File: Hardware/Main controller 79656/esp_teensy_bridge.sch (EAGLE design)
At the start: 101 parts, among them IC2 PBQ79656PAPTQ1, Q5 VISHAY_SIS862DN-T1-GE3VISHAY_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, Q6 VISHAY_SIS862DN-T1-GE3VISHAY_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, Q7 VISHAY_SIS862DN-T1-GE3VISHAY_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, Q8 VISHAY_SIS862DN-T1-GE3VISHAY_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, T2 PBHV8115X, 115, U1 MCP2562-E/SN, U2 ESP32-DEVKITC-32D, X1 5566-12

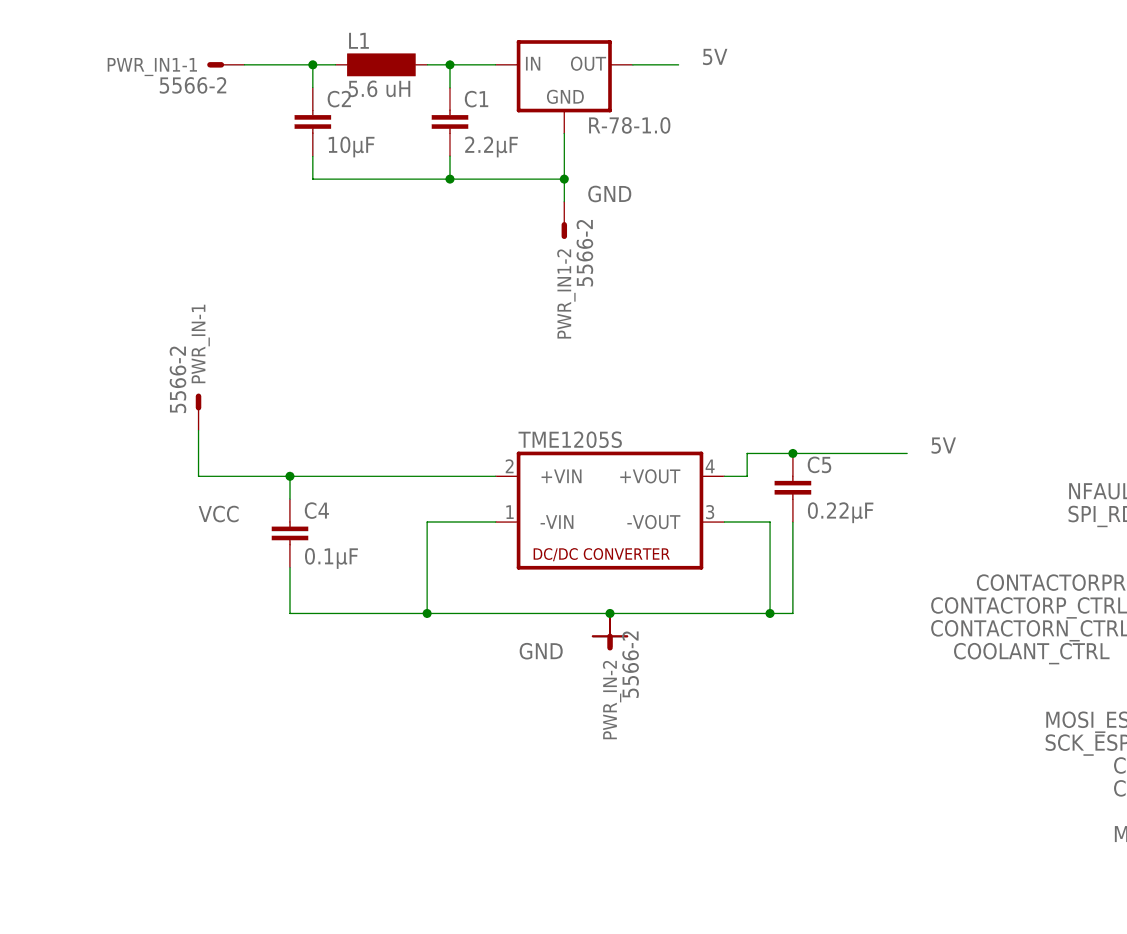
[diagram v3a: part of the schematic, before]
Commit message: buck converter layout
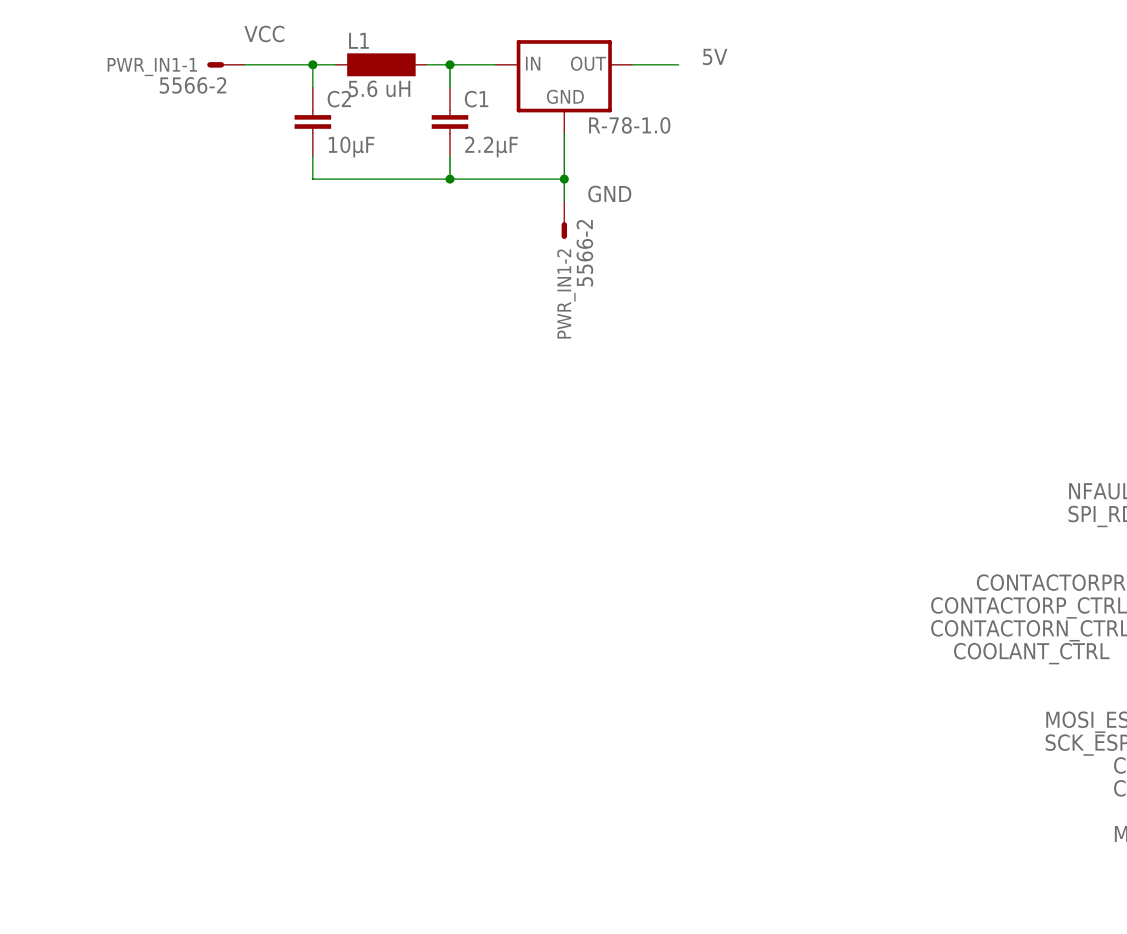
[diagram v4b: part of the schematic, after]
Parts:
- removed C4: 0.1μF, rcl:C-EUC0603
- removed C5: 0.22μF, rcl:C-EUC0603
- removed PWR_IN: 5566-2, con-molex:5566-2
- removed TME1205S: (no value), dc-dc-converter:NME
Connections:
- removed net N$36: C2.1, L1.1, PWR_IN1-1.S
- net 5V: no longer C5.1, TME1205S.+VOUT
- net GND: no longer C4.2, C5.2, PWR_IN-2.S, TME1205S.-VIN, TME1205S.-VOUT
- net VCC: now also C2.1, L1.1, PWR_IN1-1.S; no longer C4.1, PWR_IN-1.S, TME1205S.+VIN
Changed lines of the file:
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@@
 </classes>
 <parts>
-<part name="TME1205S" library="dc-dc-converter" library_urn="urn:adsk.eagle:library:208" deviceset="NME" device="" package3d_urn="urn:adsk.eagle:package:12313/1"/>
-<part name="GND1" library="supply1" library_urn="urn:adsk.eagle:library:371" deviceset="GND" device=""/>
-<part name="C5" library="rcl" library_urn="urn:adsk.eagle:library:334" deviceset="C-EU" device="C0603" package3d_urn="urn:adsk.eagle:package:23616/2" value="0.22μF"/>
-<part name="C4" library="rcl" library_urn="urn:adsk.eagle:library:334" deviceset="C-EU" device="C0603" package3d_urn="urn:adsk.eagle:package:23616/2" value="0.1μF"/>
-<part name="PWR_IN" library="con-molex" library_urn="urn:adsk.eagle:library:165" deviceset="5566-2" device="" package3d_urn="urn:adsk.eagle:package:8078583/1"/>
 <part name="COOLANT" library="con-molex" library_urn="urn:adsk.eagle:library:165" deviceset="5566-2" device="" package3d_urn="urn:adsk.eagle:package:8078583/1"/>
 <part name="CONTACTOR_N" library="con-molex" library_urn="urn:adsk.eagle:library:165" deviceset="5566-2" device="" package3d_urn="urn:adsk.eagle:package:8078583/1"/>
@@
 </plain>
 <instances>
-<instance part="TME1205S" gate="G$1" x="-30.48" y="111.76" smashed="yes">
-<attribute name="NAME" x="-40.64" y="117.475" size="1.778" layer="95"/>
-<attribute name="VALUE" x="-40.64" y="101.6" size="1.778" layer="96"/>
-</instance>
-<instance part="GND1" gate="1" x="-30.48" y="96.52" smashed="yes">
-<attribute name="VALUE" x="-40.64" y="93.98" size="1.778" layer="96"/>
-</instance>
-<instance part="C5" gate="G$1" x="-10.16" y="114.3" smashed="yes">
-<attribute name="NAME" x="-8.636" y="114.681" size="1.778" layer="95"/>
-<attribute name="VALUE" x="-8.636" y="109.601" size="1.778" layer="96"/>
-</instance>
-<instance part="C4" gate="G$1" x="-66.04" y="109.22" smashed="yes">
-<attribute name="NAME" x="-64.516" y="109.601" size="1.778" layer="95"/>
-<attribute name="VALUE" x="-64.516" y="104.521" size="1.778" layer="96"/>
-</instance>
-<instance part="PWR_IN" gate="-1" x="-76.2" y="121.92" smashed="yes" rot="R90">
-<attribute name="NAME" x="-75.438" y="124.46" size="1.524" layer="95" rot="R90"/>
-<attribute name="VALUE" x="-77.597" y="121.158" size="1.778" layer="96" rot="R90"/>
-</instance>
-<instance part="PWR_IN" gate="-2" x="-30.48" y="96.52" smashed="yes" rot="R270">
-<attribute name="NAME" x="-31.242" y="93.98" size="1.524" layer="95" rot="R270"/>
-<attribute name="VALUE" x="-29.083" y="97.282" size="1.778" layer="96" rot="R270"/>
-</instance>
 <instance part="COOLANT" gate="-1" x="-119.38" y="71.12" smashed="yes">
 <attribute name="NAME" x="-116.84" y="70.358" size="1.524" layer="95"/>
@@
 <nets>
 <net name="GND" class="0">
-<segment>
-<pinref part="TME1205S" gate="G$1" pin="-VIN"/>
-<wire x1="-50.8" y1="109.22" x2="-43.18" y2="109.22" width="0.1524" layer="91"/>
-<wire x1="-50.8" y1="109.22" x2="-50.8" y2="99.06" width="0.1524" layer="91"/>
-<wire x1="-50.8" y1="99.06" x2="-30.48" y2="99.06" width="0.1524" layer="91"/>
-<wire x1="-30.48" y1="99.06" x2="-12.7" y2="99.06" width="0.1524" layer="91"/>
-<pinref part="GND1" gate="1" pin="GND"/>
-<junction x="-30.48" y="99.06"/>
-<pinref part="C4" gate="G$1" pin="2"/>
-<wire x1="-66.04" y1="104.14" x2="-66.04" y2="99.06" width="0.1524" layer="91"/>
-<wire x1="-66.04" y1="99.06" x2="-50.8" y2="99.06" width="0.1524" layer="91"/>
-<junction x="-50.8" y="99.06"/>
-<pinref part="TME1205S" gate="G$1" pin="-VOUT"/>
-<wire x1="-17.78" y1="109.22" x2="-12.7" y2="109.22" width="0.1524" layer="91"/>
-<wire x1="-12.7" y1="109.22" x2="-12.7" y2="99.06" width="0.1524" layer="91"/>
-<wire x1="-12.7" y1="99.06" x2="-10.16" y2="99.06" width="0.1524" layer="91"/>
-<junction x="-12.7" y="99.06"/>
-<pinref part="C5" gate="G$1" pin="2"/>
-<wire x1="-10.16" y1="99.06" x2="-10.16" y2="109.22" width="0.1524" layer="91"/>
-<pinref part="PWR_IN" gate="-2" pin="S"/>
-</segment>
 <segment>
 <wire x1="-129.54" y1="63.5" x2="-129.54" y2="60.96" width="0.1524" layer="91"/>
@@
 <net name="5V" class="0">
 <segment>
-<pinref part="TME1205S" gate="G$1" pin="+VOUT"/>
-<wire x1="-17.78" y1="114.3" x2="-15.24" y2="114.3" width="0.1524" layer="91"/>
-<wire x1="-15.24" y1="114.3" x2="-15.24" y2="116.84" width="0.1524" layer="91"/>
-<pinref part="C5" gate="G$1" pin="1"/>
-<wire x1="-15.24" y1="116.84" x2="-10.16" y2="116.84" width="0.1524" layer="91"/>
-<wire x1="-10.16" y1="116.84" x2="2.54" y2="116.84" width="0.1524" layer="91"/>
-<junction x="-10.16" y="116.84"/>
-<label x="5.08" y="116.84" size="1.778" layer="95"/>
-</segment>
-<segment>
 <pinref part="U$3" gate="G$1" pin="VIN"/>
 <wire x1="71.12" y1="127" x2="71.12" y2="132.08" width="0.1524" layer="91"/>
@@
 <wire x1="-121.92" y1="-10.16" x2="-124.46" y2="-10.16" width="0.1524" layer="91"/>
 <label x="-124.46" y="-10.16" size="1.778" layer="95"/>
-</segment>
-<segment>
-<wire x1="-76.2" y1="119.38" x2="-76.2" y2="114.3" width="0.1524" layer="91"/>
-<pinref part="TME1205S" gate="G$1" pin="+VIN"/>
-<wire x1="-76.2" y1="114.3" x2="-66.04" y2="114.3" width="0.1524" layer="91"/>
-<pinref part="C4" gate="G$1" pin="1"/>
-<wire x1="-66.04" y1="114.3" x2="-43.18" y2="114.3" width="0.1524" layer="91"/>
-<wire x1="-66.04" y1="111.76" x2="-66.04" y2="114.3" width="0.1524" layer="91"/>
-<junction x="-66.04" y="114.3"/>
-<label x="-76.2" y="109.22" size="1.778" layer="95"/>
-<pinref part="PWR_IN" gate="-1" pin="S"/>
 </segment>
 <segment>
@@
 <wire x1="-60.96" y1="-218.44" x2="-71.12" y2="-218.44" width="0.1524" layer="91"/>
 <label x="-71.12" y="-218.44" size="1.778" layer="95"/>
+</segment>
+<segment>
+<pinref part="C2" gate="G$1" pin="1"/>
+<wire x1="-63.5" y1="157.48" x2="-63.5" y2="160.02" width="0.1524" layer="91"/>
+<pinref part="L1" gate="G$1" pin="1"/>
+<wire x1="-63.5" y1="160.02" x2="-60.96" y2="160.02" width="0.1524" layer="91"/>
+<pinref part="PWR_IN1" gate="-1" pin="S"/>
+<wire x1="-63.5" y1="160.02" x2="-71.12" y2="160.02" width="0.1524" layer="91"/>
+<junction x="-63.5" y="160.02"/>
+<label x="-71.12" y="162.56" size="1.778" layer="95"/>
 </segment>
 </net>
@@
 </segment>
 </net>
-<net name="N$36" class="0">
-<segment>
-<pinref part="C2" gate="G$1" pin="1"/>
-<wire x1="-63.5" y1="157.48" x2="-63.5" y2="160.02" width="0.1524" layer="91"/>
-<pinref part="L1" gate="G$1" pin="1"/>
-<wire x1="-63.5" y1="160.02" x2="-60.96" y2="160.02" width="0.1524" layer="91"/>
-<pinref part="PWR_IN1" gate="-1" pin="S"/>
-<wire x1="-63.5" y1="160.02" x2="-71.12" y2="160.02" width="0.1524" layer="91"/>
-<junction x="-63.5" y="160.02"/>
-</segment>
-</net>

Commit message: Mainboard fixes
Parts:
- removed R-78-1.0: (no value), v-reg:78XXS
- added PS1: R-785.0-1.0, R-785.0-1.0:R-785.0-1.0
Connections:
- net 5V: now also PS1.+VOUT; no longer R-78-1.0.OUT
- net GND: now also PS1.GND, U2.GND2, U2.GND3; no longer R-78-1.0.GND
- net N$16: now also PS1.+VIN; no longer R-78-1.0.IN
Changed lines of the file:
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@@
 <part name="R9" library="rcl" library_urn="urn:adsk.eagle:library:334" deviceset="R-US_" device="R0805" package3d_urn="urn:adsk.eagle:package:23553/2"/>
 <part name="U$1" library="TB0108" deviceset="TXB0108PW" device="SMD"/>
-<part name="R-78-1.0" library="v-reg" library_urn="urn:adsk.eagle:library:409" deviceset="78XXS" device="" package3d_urn="urn:adsk.eagle:package:30342/1"/>
 <part name="C1" library="rcl" library_urn="urn:adsk.eagle:library:334" deviceset="C-EU" device="C0603" package3d_urn="urn:adsk.eagle:package:23616/2" value="2.2μF"/>
 <part name="C2" library="rcl" library_urn="urn:adsk.eagle:library:334" deviceset="C-EU" device="C0603" package3d_urn="urn:adsk.eagle:package:23616/2" value="10μF"/>
 <part name="L1" library="inductor-neosid" library_urn="urn:adsk.eagle:library:241" deviceset="SD8" device="" package3d_urn="urn:adsk.eagle:package:14649/1" value="5.6 uH"/>
 <part name="PWR_IN1" library="con-molex" library_urn="urn:adsk.eagle:library:165" deviceset="5566-2" device="" package3d_urn="urn:adsk.eagle:package:8078583/1"/>
+<part name="PS1" library="R-785.0-1.0" deviceset="R-785.0-1.0" device=""/>
 </parts>
 <sheets>
@@
 <attribute name="VALUE" x="88.9" y="-121.92" size="1.27" layer="96" rot="R180"/>
 </instance>
-<instance part="R-78-1.0" gate="1" x="-35.56" y="160.02" smashed="yes">
-<attribute name="NAME" x="-33.02" y="152.4" size="1.778" layer="95"/>
-<attribute name="VALUE" x="-33.02" y="149.86" size="1.778" layer="96"/>
-</instance>
 <instance part="C1" gate="G$1" x="-48.26" y="154.94" smashed="yes">
 <attribute name="NAME" x="-46.736" y="155.321" size="1.778" layer="95"/>
@@
 <attribute name="NAME" x="-36.322" y="139.7" size="1.524" layer="95" rot="R270"/>
 <attribute name="VALUE" x="-34.163" y="143.002" size="1.778" layer="96" rot="R270"/>
+</instance>
+<instance part="PS1" gate="G$1" x="-33.02" y="170.18" smashed="yes">
+<attribute name="NAME" x="-43.1839" y="176.5379" size="1.77938125" layer="95"/>
+<attribute name="VALUE" x="-43.1814" y="162.5573" size="1.77848125" layer="96"/>
 </instance>
 </instances>
@@
 </segment>
 <segment>
-<pinref part="R-78-1.0" gate="1" pin="GND"/>
-<wire x1="-35.56" y1="152.4" x2="-35.56" y2="147.32" width="0.1524" layer="91"/>
 <wire x1="-35.56" y1="147.32" x2="-48.26" y2="147.32" width="0.1524" layer="91"/>
 <pinref part="C1" gate="G$1" pin="2"/>
@@
 <junction x="-35.56" y="147.32"/>
 <label x="-33.02" y="144.78" size="1.778" layer="95"/>
+<pinref part="PS1" gate="G$1" pin="GND"/>
+<wire x1="-35.56" y1="147.32" x2="-17.78" y2="147.32" width="0.1524" layer="91"/>
+<wire x1="-17.78" y1="147.32" x2="-17.78" y2="167.64" width="0.1524" layer="91"/>
+</segment>
+<segment>
+<pinref part="U2" gate="G$1" pin="GND3"/>
+<wire x1="73.66" y1="7.62" x2="78.74" y2="7.62" width="0.1524" layer="91"/>
+<label x="73.66" y="7.62" size="1.778" layer="95"/>
+</segment>
+<segment>
+<pinref part="U2" gate="G$1" pin="GND2"/>
+<wire x1="73.66" y1="-7.62" x2="78.74" y2="-7.62" width="0.1524" layer="91"/>
+<label x="73.66" y="-7.62" size="1.778" layer="95"/>
 </segment>
 </net>
@@
 </segment>
 <segment>
-<pinref part="R-78-1.0" gate="1" pin="OUT"/>
 <wire x1="-27.94" y1="160.02" x2="-22.86" y2="160.02" width="0.1524" layer="91"/>
 <label x="-20.32" y="160.02" size="1.778" layer="95"/>
+<pinref part="PS1" gate="G$1" pin="+VOUT"/>
+<wire x1="-27.94" y1="160.02" x2="-27.94" y2="172.72" width="0.1524" layer="91"/>
+<wire x1="-27.94" y1="172.72" x2="-17.78" y2="172.72" width="0.1524" layer="91"/>
 </segment>
 </net>
@@
 <net name="N$16" class="0">
 <segment>
-<pinref part="R-78-1.0" gate="1" pin="IN"/>
 <pinref part="C1" gate="G$1" pin="1"/>
 <wire x1="-48.26" y1="157.48" x2="-48.26" y2="160.02" width="0.1524" layer="91"/>
@@
 <wire x1="-50.8" y1="160.02" x2="-48.26" y2="160.02" width="0.1524" layer="91"/>
 <junction x="-48.26" y="160.02"/>
-</segment>
-</net>
+<pinref part="PS1" gate="G$1" pin="+VIN"/>
+<wire x1="-48.26" y1="172.72" x2="-43.18" y2="172.72" width="0.1524" layer="91"/>
+<wire x1="-43.18" y1="172.72" x2="-43.18" y2="160.02" width="0.1524" layer="91"/>
+</segment>
+</net>

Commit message: BMS V3 hardware
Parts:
- removed C2: 10μF, rcl:C-EUC0603
- removed C6: 0.1μF, rcl:C-EUC0603
- removed CAN: 5566-2, con-molex:5566-2
- removed CTSREF2: 1uf, rcl:C-EUC0603
- removed L1: 5.6 uH, inductor-neosid:SD8
- removed TEMPH: 5566-16, con-molex:5566-16
- removed TEMPR10, TEMPR11, TEMPR12, TEMPR13, TEMPR14, TEMPR15, TEMPR16, TEMPR9: 10k, rcl:R-US_R0603
- added C3, C4: 0.1μF, rcl:C-EUC0603
- added CAN1, CAN2, CAN3: 5566-2, con-molex:5566-2
- added R10, R19: 120, rcl:R-US_R0603
- added U3, U4, U5: CAN_TRANSCAN_TRANS, NFR23_v1.1:CAN_TRANSCAN_TRANS
- C1: value 2.2μF -> 0.1μF
- CCOMHN, CCOMHP, CCOMLN, CCOMLP: device rcl:C-EUC0603 -> rcl:C-EU050-035X075
- PS1: value R-785.0-1.0 -> TSR_1-2450; device R-785.0-1.0:R-785.0-1.0 -> dcdc_5v:TSR_1-2450
- U1: value MCP2562-E/SN -> CAN_TRANSCAN_TRANS; device MCP2562-E_SN:MCP2562-E/SN -> NFR23_v1.1:CAN_TRANSCAN_TRANS
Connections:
- removed net CANH: CAN-1.S, R8.1, U1.CANH
- removed net CANL: CAN-2.S, R8.2, U1.CANL
- removed net CRX: U$3.30-CRX3, U1.RXD
- removed net CS0: U$3.38-A14/CS/IN1
- removed net CSTBY: U$3.29-TX7, U1.STBY
- removed net CTX: U$3.31-CTX3, U1.TXD
- removed net MISO: U$3.12-MISO/MQSL
- removed net MOSI: U$3.11-MOSI/CTX1
- removed net N$16: C1.1, L1.2, PS1.+VIN
- removed net N$30: R17.1, U2.IO5
- removed net SCK: U$3.13-SCK/LED
- removed net SPI_RDY: U$3.17-A3/TX4/SDA1
- removed net TEMP12: IC2.GPIO4, TEMPH-4.S, TEMPR12.2
- removed net TSREF-1: CTSREF2.2, IC2.TSREF, TEMPR10.1, TEMPR11.1, TEMPR12.1, TEMPR13.1, TEMPR14.1, TEMPR15.1, TEMPR16.1, TEMPR9.1
- new net CANH1: CAN1-1.S, R10.1, U5.CANH
- new net CANH2: CAN2-1.S, R8.1, U1.CANH
- new net CANH3: CAN3-1.S, R19.1, U3.CANH, U4.CANH
- new net CANL1: CAN1-2.S, R10.2, U5.CANL
- new net CANL2: CAN2-2.S, R8.2, U1.CANL
- new net CANL3: CAN3-2.S, R19.2, U3.CANL, U4.CANL
- new net CRX1: U$3.23-A9/CRX1/MCLK1, U5.CANRX
- new net CRX2: U$3.0-RX1/CS1/CRX2, U1.CANRX
- new net CRX3: U$3.30-CRX3, U3.CANRX
- new net CTX1: U$3.22-A8/CTX1, U5.CANTX
- new net CTX2: U$3.1-TX1/MISO1/CTX2, U1.CANTX
- new net CTX3: U$3.31-CTX3, U3.CANTX
- new net ESPCANRX: U2.IO4, U4.CANRX
- new net ESPCANTX: U2.IO5, U4.CANTX
- new net N$11: R17.1, U2.IO22
- new net N$41: IC2.TSREF
- net 3V3: now also C1.2, C3.2, C4.2, C7.2, U1.VCC, U3.VCC, U4.VCC, U5.VCC; no longer C7.1, U1.VIO
- net 5V: no longer C6.1, U1.VDD
- net CONTACTORN_CTRL: now also U$3.10-CS/MQSR; no longer U$3.22-A8/CTX1
- net COOLANT_CTRL: now also U$3.11-MOSI/CTX1; no longer U$3.23-A9/CRX1/MCLK1
- net GND: now also C1.1, C3.1, C4.1, C7.1, U1.GND, U1.RS, U3.GND, U3.RS, U4.GND, U4.RS, U5.GND, U5.RS; no longer C1.2, C2.2, C6.2, C7.2, CTSREF2.1, TEMPH-10.S, TEMPH-11.S, TEMPH-12.S, TEMPH-13.S, TEMPH-14.S, TEMPH-15.S, TEMPH-16.S, TEMPH-9.S, U1.VSS
- net NFAULT: now also IC2.NFAULT
- net RX_ESP: now also U$3.29-TX7; no longer U$3.1-TX1/MISO1/CTX2
- net TEMP10: no longer TEMPH-2.S, TEMPR10.2
- net TEMP11: no longer TEMPH-3.S, TEMPR11.2
- net TEMP13: no longer TEMPH-5.S, TEMPR13.2
- net TEMP14: no longer TEMPH-6.S, TEMPR14.2
- net TEMP15: no longer TEMPH-7.S, TEMPR15.2
- net TEMP16: no longer TEMPH-8.S, TEMPR16.2
- net TEMP9: no longer TEMPH-1.S, TEMPR9.2
- net TX_ESP: now also U$3.28-RX7; no longer U$3.0-RX1/CS1/CRX2
- net VCC: now also PS1.+VIN; no longer C2.1, L1.1
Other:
- moved on the sheet: C1, C7, R8

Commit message: Labelled HV/LV on mainboard
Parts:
- removed CAN1, CAN2, CAN3, COMH, COML, CONTACTOR_N, CONTACTOR_P, CONTACTOR_PRECHARGE, COOLANT, PWR_IN1: 5566-2, con-molex:5566-2
- removed Q5, Q6, Q7, Q8: VISHAY_SIS862DN-T1-GE3VISHAY_SIS862DN-T1-GE3_0_0, Vishay - SIS862DN-T1-GE3:VISHAY_SIS862DN-T1-GE3VISHAY_SIS862DN-T1-GE3_0_0
- removed X1: 5566-12, con-molex:5566-12
- added CVCC: 10uf, rcl:C-EUC0805
- added J1, J2: DF11-4DP-2DSA(24), hirose_connectors:DF11-4DP-2DSA(24)
- added J3: TE_AMP_SURESEAL_26, TE_Sureseal:TE_AMP_SURESEAL_26
- added Q1, Q2, Q3, Q4: EPC2065, EPCGaNFET:EPC2065
- added R20, R21, R22, R23: 300, rcl:R-US_R0603
- added R24: 6k, rcl:R-US_R0603
- added R25: 1k, rcl:R-US_R0603
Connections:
- removed net N$12: CONTACTOR_P-2.S, Q7.D
- removed net N$14: U$3.14-A0/TX3/SPDIF_OUT, X1-1.S
- removed net N$17: U$3.15-A1/RX3/SPDIF_IN, X1-2.S
- removed net N$18: U$3.18-A4/SDA0, X1-3.S
- removed net N$19: U$3.19-A5/SCL0, X1-4.S
- removed net N$2: CONTACTOR_N-2.S, Q6.D
- removed net N$20: U$3.24-A10/TX6/SCL2, X1-5.S
- removed net N$21: U$3.25-A11/RX6/SDA2, X1-6.S
- removed net N$22: U$3.40-A16/CS1, X1-7.S
- removed net N$23: U$3.32-OUT1B, X1-8.S
- removed net N$24: U$3.9-OUT1C, X1-9.S
- removed net N$25: U$3.6-OUT1D, X1-10.S
- removed net N$26: U$3.33-MCLK2, X1-12.S
- removed net N$27: U$3.2-OUT2, X1-11.S
- removed net N$5: COOLANT-2.S, Q5.D
- removed net N$6: CONTACTOR_PRECHARGE-2.S, Q8.D
- new net CONTACTORN_OUT: J3.24, Q3.3, Q3.5, Q3.7, R13.1
- new net CONTACTORPRECHARGE_OUT: J3.26, Q1.3, Q1.5, Q1.7, R11.1
- new net CONTACTORP_OUT: J3.25, Q2.3, Q2.5, Q2.7, R12.1
- new net COOLING_OUT: J3.17, J3.18, J3.19, Q4.3, Q4.5, Q4.7, R14.1
- new net N$15: Q1.1, R20.1
- new net N$16: Q2.1, R21.1
- new net N$30: Q3.1, R23.1
- new net N$36: Q4.1, R22.1
- new net NFAULT_3V3: U$1.A3, U$3.16-A2/RX4/SCL1
- new net SHUTDOWN_IN: J3.11, R24.2
- new net SHUTDOWN_SIGNAL: R24.1, R25.2, U$3.38-A14/CS/IN1
- net CANH1: now also J3.4; no longer CAN1-1.S
- net CANH2: now also J3.3; no longer CAN2-1.S
- net CANH3: now also J3.2; no longer CAN3-1.S
- net CANL1: now also J3.10; no longer CAN1-2.S
- net CANL2: now also J3.9; no longer CAN2-2.S
- net CANL3: now also J3.8; no longer CAN3-2.S
- net COMHN: now also J1.4; no longer COMH-1.S
- net COMHP: now also J1.3; no longer COMH-2.S
- net COMLN: now also J2.1; no longer COML-1.S
- net COMLP: now also J2.2; no longer COML-2.S
- net CONTACTORN_CTRL: now also R23.2; no longer Q6.G, R13.1
- net CONTACTORPRECHARGE_CTRL: now also R20.2; no longer Q8.G, R11.1
- net CONTACTORP_CTRL: now also R21.2; no longer Q7.G, R12.1
- net COOLANT_CTRL: now also R22.2; no longer Q5.G, R14.1
- net GND: now also CVCC.1, J3.12, J3.13, J3.5, J3.6, J3.7, Q1.2, Q1.4, Q1.6, Q1.8, Q2.2, Q2.4, Q2.6, Q2.8, Q3.2, Q3.4, Q3.6, Q3.8, Q4.2, Q4.4, Q4.6, Q4.8, R25.1; no longer PWR_IN1-2.S, Q5.1_S, Q5.2_S, Q5.3_S, Q6.1_S, Q6.2_S, Q6.3_S, Q7.1_S, Q7.2_S, Q7.3_S, Q8.1_S, Q8.2_S, Q8.3_S
- net N$13: now also LED1.C, R11.2; no longer LED4.A, R14.2
- net N$130: now also CVCC.2
- net N$3: now also LED4.C, R14.2; no longer LED1.A, R11.2
- net N$4: now also LED3.C, R13.2; no longer LED2.A, R12.2
- net N$9: now also LED2.C, R12.2; no longer LED3.A, R13.2
- net NFAULT: now also U$1.B3; no longer U$3.16-A2/RX4/SCL1
- net VCC: now also J3.1, LED1.A, LED2.A, LED3.A, LED4.A; no longer CONTACTOR_N-1.S, CONTACTOR_P-1.S, CONTACTOR_PRECHARGE-1.S, COOLANT-1.S, LED1.C, LED2.C, LED3.C, LED4.C, PWR_IN1-1.S
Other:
- moved on the sheet: LED1, LED2, LED3, LED4, R1, R5, R6, R7
